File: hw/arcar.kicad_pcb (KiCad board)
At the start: 2 copper layers, 74 parts, among them J1 USB_B_Micro, J2 GPIO, J3 MOTOR, J4 POWER, M1 screw, M2 screw, M3 screw, P1 AVR_ISP_02X03, SW1 SW_Push, U1 USBLC6-2SC6, U10 MCP1826S, U2 ATMEGA328PB-AU, U3 CP2102, U4 ULN2003A, U5 LSM9DS1, U6 ULN2003A, U7 TLE52062GAUMA1, U8 RN4871, U9 MCP16301H

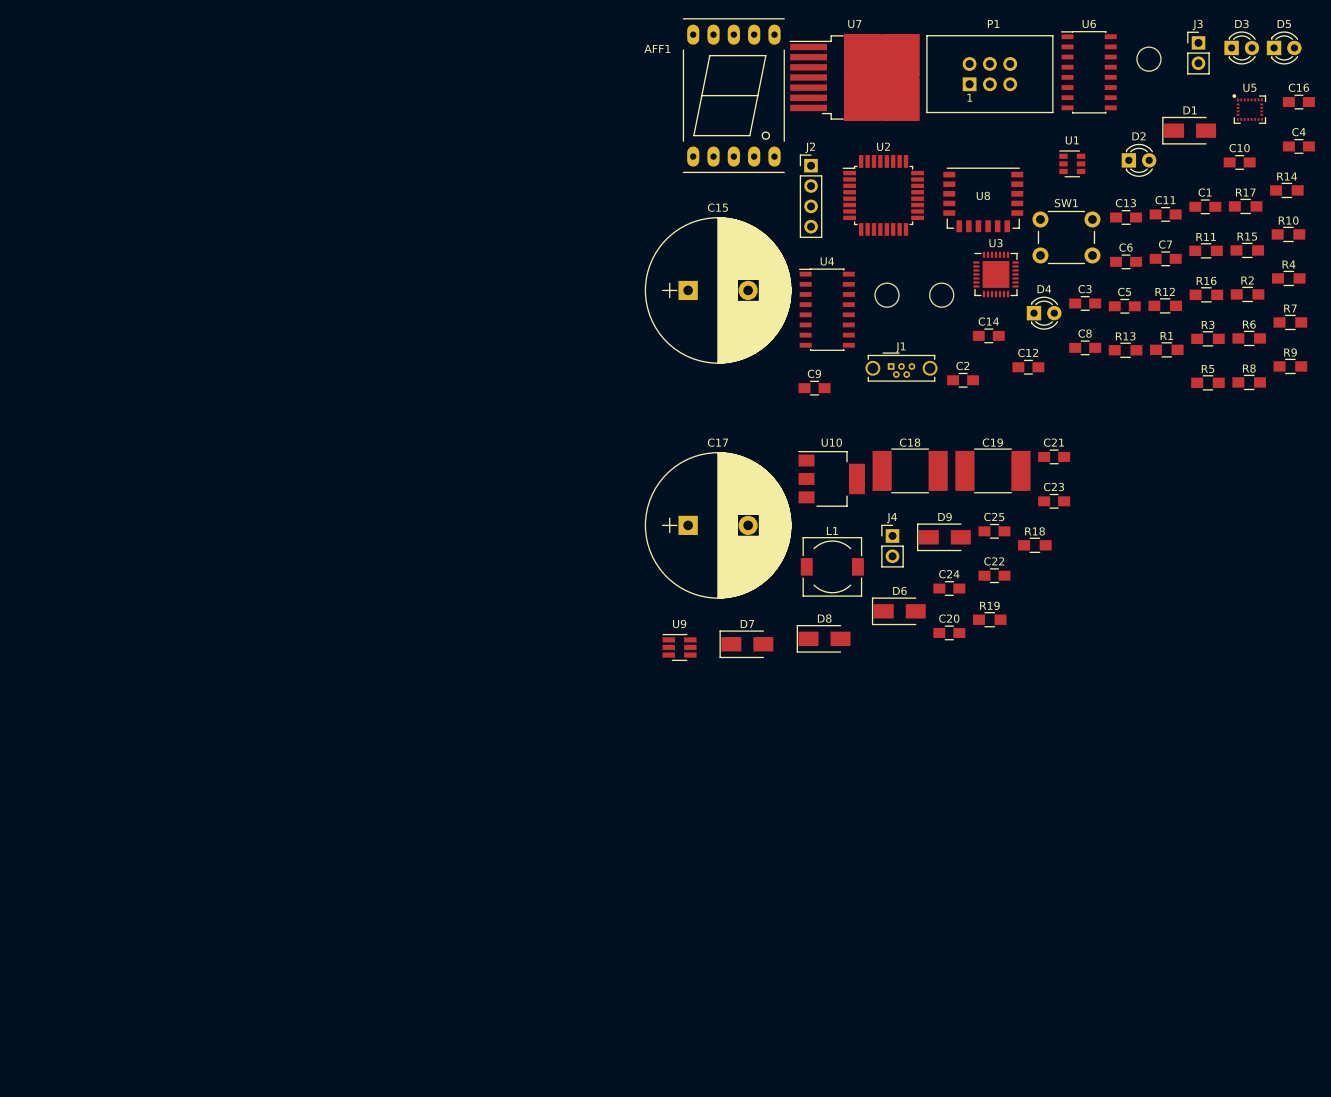
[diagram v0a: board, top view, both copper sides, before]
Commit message: reduced schematic
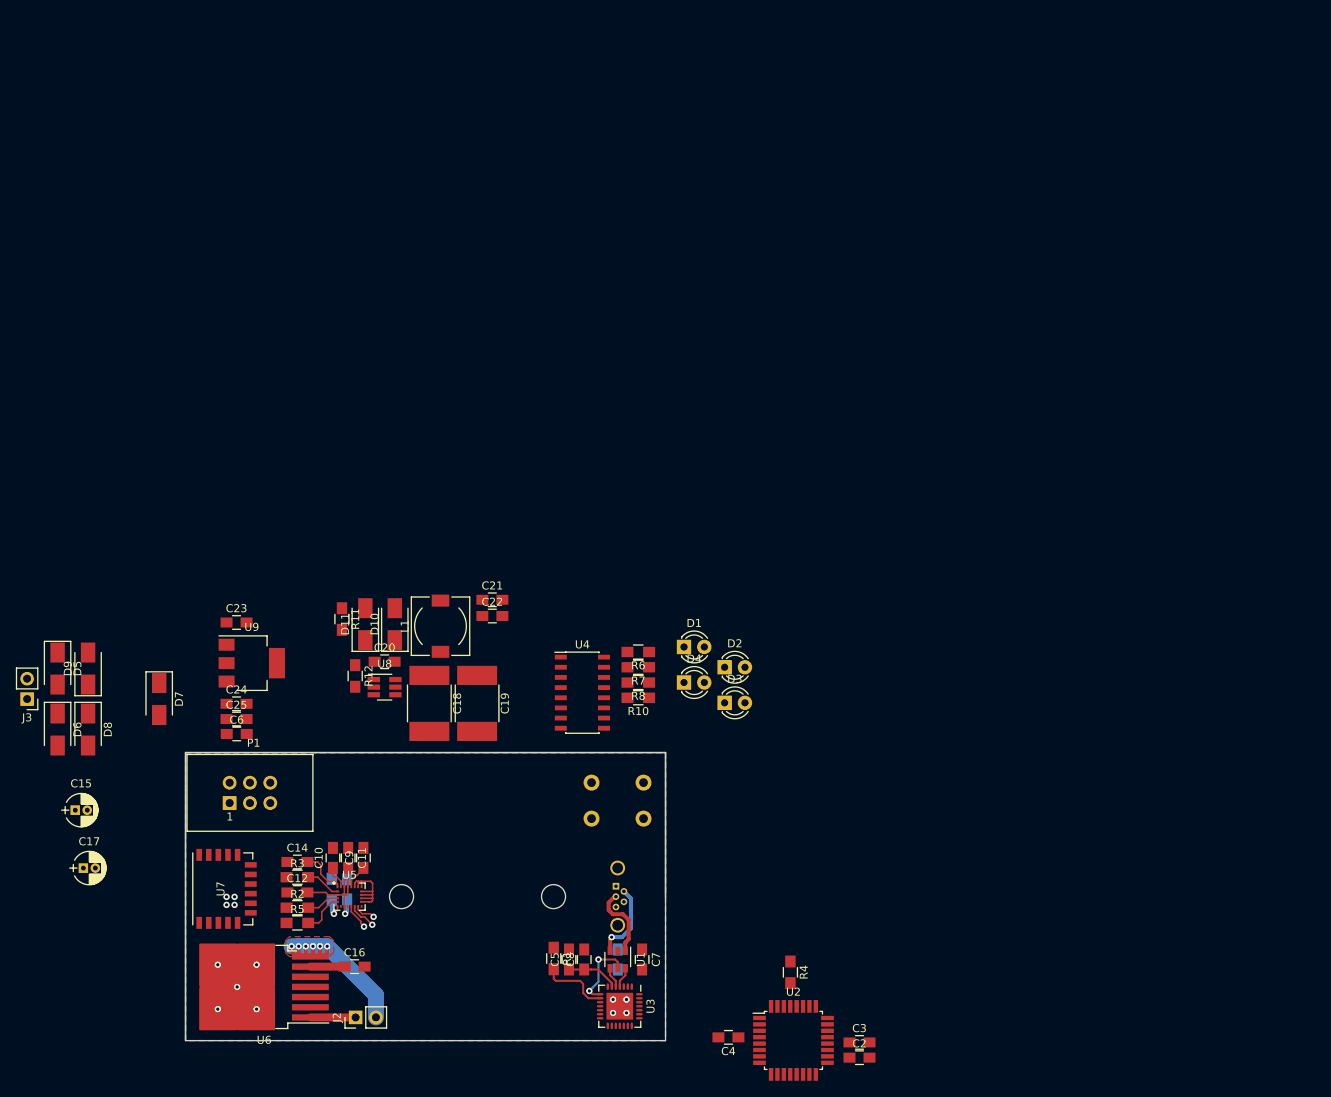
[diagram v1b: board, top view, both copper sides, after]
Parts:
- removed AFF1: LTS-6960HR, Displays_7-Segment:7SegmentLED_LTS6760_LTS6780
- removed J4: POWER, Socket_Strips:Socket_Strip_Straight_1x02_Pitch2.54mm
- removed M3: screw, wyk_mech:screw_M3
- removed R13: 10k, Resistors_SMD:R_0805_HandSoldering
- removed R14, R15, R16, R17: 330R, Resistors_SMD:R_0805_HandSoldering
- removed R18: 330k, Resistors_SMD:R_0805_HandSoldering
- removed R19: 56k, Resistors_SMD:R_0805_HandSoldering
- removed U10: MCP1826S, TO_SOT_Packages_SMD:SOT-223-3Lead_TabPin2
- added D10: SK32SMA, Diodes_SMD:D_SMA, F.Cu at (53.2, 115.9)
- added D11: SK32SMA, Diodes_SMD:D_SMA, F.Cu at (49.5, 115.9)
- C1, C13, J1, SW1: moved to B.Cu
- C15, C17: footprint Capacitors_THT:CP_Radial_D18.0mm_P7.50mm -> Capacitors_THT:CP_Radial_D4.0mm_P1.50mm
- D1: value SK32SMA -> LED; footprint Diodes_SMD:D_SMA -> LEDs:LED_D3.0mm_FlatTop
- D5: value LED -> SK32SMA; footprint LEDs:LED_D3.0mm_FlatTop -> Diodes_SMD:D_SMA
- J2: value GPIO -> MOTOR; footprint Pin_Headers:Pin_Header_Straight_1x04_Pitch2.54mm -> Pin_Headers:Pin_Header_Straight_1x02_Pitch2.54mm
- J3: value MOTOR -> POWER
- R11: value 330R -> 220k
- R12: value 330R -> 22k
- R2: value 10k -> 4k7
- R4: value 4k7 -> 10k
- R9: value 330R -> 10k; moved to B.Cu
- U6: value ULN2003A -> TLE52062GAUMA1; footprint Housings_SOIC:SOIC-16_3.9x9.9mm_Pitch1.27mm -> TO_SOT_Packages_SMD:TO-263-7_TabPin4
- U7: value TLE52062GAUMA1 -> RN4871; footprint TO_SOT_Packages_SMD:TO-263-7_TabPin4 -> wyk_rf_modules:RN4871
- U8: value RN4871 -> MCP16301H; footprint wyk_rf_modules:RN4871 -> TO_SOT_Packages_SMD:SOT-23-6_Handsoldering
- U9: value MCP16301H -> MCP1826S; footprint TO_SOT_Packages_SMD:SOT-23-6_Handsoldering -> TO_SOT_Packages_SMD:SOT-223-3Lead_TabPin2
- moved D5 170.7 mm to (11.0, 121.5), turned to 270 degrees
- moved J3 167.8 mm to (7.20, 125.3), turned to 180 degrees
- moved C16 160.0 mm to (48.1, 158.8)
- moved U6 154.0 mm to (36.8, 161.3), turned to 180 degrees
- moved U5 149.5 mm to (47.5, 150.0)
- moved C10 142.8 mm to (45.4, 145.2), turned to 90 degrees
- moved R2 141.4 mm to (41.0, 151.4)
- moved R9 136.5 mm to (45.3, 149.1), turned to 270 degrees
- moved R5 132.3 mm to (41.0, 153.3)
- moved C4 132.2 mm to (94.9, 167.6), turned to 180 degrees
- moved R3 132.2 mm to (41.0, 147.6)
- moved C11 130.0 mm to (47.3, 145.2), turned to 270 degrees
- moved P1 128.9 mm to (32.5, 138.3)
- moved C13 128.6 mm to (47.2, 149.1), turned to 270 degrees
- moved M2 128.4 mm to (73.0, 150.0)
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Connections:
- net Net-(J1-Pad2) renamed /D-
- net Net-(J1-Pad3) renamed /D+
- net Net-(U1-Pad4) renamed /D2-
- net Net-(U1-Pad6) renamed /D2+
- C21 pad 1: +5V5 -> +5V
- C22 pad 1: +5V5 -> +5V
- C23 pad 1: +5V5 -> +5V
- D1 pad 1: +5V5 -> Net-(D1-Pad1)
- D1 pad 2: Net-(D1-Pad2) -> VCC
- D5 pad 1: Net-(D5-Pad1) -> VCC
- D5 pad 2: VCC -> Net-(D5-Pad2)
- D6 pad 1: VCC -> Net-(D5-Pad2)
- D6 pad 2: Net-(D6-Pad2) -> GND
- D7 pad 1: Net-(C17-Pad1) -> VCC
- D7 pad 2: VCC -> Net-(D7-Pad2)
- D8 pad 1: Net-(C20-Pad2) -> Net-(D7-Pad2)
- D9 pad 1: Net-(C20-Pad1) -> Net-(C17-Pad1)
- D9 pad 2: +5V5 -> VCC
- J2 pad 1: /GPIO1 -> Net-(J2-Pad1)
- J2 pad 2: /GPIO2 -> Net-(J2-Pad2)
- J3 pad 1: Net-(J3-Pad1) -> Net-(D7-Pad2)
- J3 pad 2: Net-(J3-Pad2) -> Net-(D5-Pad2)
- L1 pad 2: +5V5 -> +5V
- P1 pad 2: Net-(D1-Pad2) -> +5V
- R10 pad 1: Net-(AFF1-Pad1) -> Net-(D4-Pad1)
- R11 pad 1: Net-(AFF1-Pad9) -> +5V
- R12 pad 1: Net-(AFF1-Pad10) -> Net-(R11-Pad2)
- R12 pad 2: Net-(R12-Pad2) -> GND
- R2 pad 2: /~RST -> /SDA
- R3 pad 2: /SDA -> /SCL
- R4 pad 2: /SCL -> /~RST
- R6 pad 1: Net-(AFF1-Pad7) -> Net-(D1-Pad1)
- R7 pad 1: Net-(AFF1-Pad6) -> Net-(D2-Pad1)
- R8 pad 1: Net-(AFF1-Pad4) -> Net-(D3-Pad1)
- R9 pad 1: Net-(AFF1-Pad2) -> +3V3
- U2 pad 10: /SEG_D -> Net-(U2-Pad10)
- U2 pad 11: /SEG_E -> Net-(U2-Pad11)
- U2 pad 19: /SEG_F -> Net-(U2-Pad19)
- U2 pad 22: /SEG_G -> Net-(U2-Pad22)
- U2 pad 3: /SEG_A -> Net-(U2-Pad3)
- U2 pad 6: /SEG_B -> Net-(U2-Pad6)
- U2 pad 7: /GPIO1 -> Net-(U2-Pad7)
- U2 pad 8: /GPIO2 -> Net-(U2-Pad8)
- U2 pad 9: /SEG_C -> Net-(U2-Pad9)
- U3 pad 7: +5V -> Net-(U3-Pad7)
- U4 pad 1: /SEG_A -> /FL_LED
- U4 pad 10: Net-(R12-Pad2) -> Net-(U4-Pad10)
- U4 pad 11: Net-(R11-Pad2) -> Net-(U4-Pad11)
- U4 pad 12: Net-(R10-Pad2) -> Net-(U4-Pad12)
- U4 pad 13: Net-(R9-Pad2) -> Net-(R10-Pad2)
- U4 pad 2: /SEG_B -> /FR_LED
- U4 pad 3: /SEG_C -> /BL_LED
- U4 pad 4: /SEG_D -> /BR_LED
- U4 pad 5: /SEG_E -> GND
- U4 pad 6: /SEG_F -> GND
- U4 pad 7: /SEG_G -> GND
- U4 pad 9: VCC -> Net-(U4-Pad9)
- U5 pad 6: Net-(R13-Pad2) -> Net-(R9-Pad2)
- U6 pad 1: /FL_LED -> Net-(J2-Pad1)
- U6 pad 2: /FR_LED -> /MOTOR_ERR
- U6 pad 3: /BL_LED -> /MOTOR_PWM1
- U6 pad 4: /BR_LED -> GND
- U6 pad 5: GND -> /MOTOR_PWM2
- U6 pad 6: GND -> VCC
- U6 pad 7: GND -> Net-(J2-Pad2)
- U7 pad 1: Net-(J3-Pad1) -> Net-(U7-Pad1)
- U7 pad 2: /MOTOR_ERR -> GND
- U7 pad 3: /MOTOR_PWM1 -> Net-(U7-Pad3)
- U7 pad 4: GND -> Net-(U7-Pad4)
- U7 pad 5: /MOTOR_PWM2 -> Net-(U7-Pad5)
- U7 pad 6: VCC -> Net-(U7-Pad6)
- U7 pad 7: Net-(J3-Pad2) -> /TX
- U8 pad 1: Net-(U8-Pad1) -> Net-(C20-Pad1)
- U8 pad 3: Net-(U8-Pad3) -> Net-(R11-Pad2)
- U8 pad 4: Net-(U8-Pad4) -> Net-(C17-Pad1)
- U8 pad 5: Net-(U8-Pad5) -> Net-(C17-Pad1)
- U8 pad 6: Net-(U8-Pad6) -> Net-(C20-Pad2)
- U9 pad 1: Net-(C20-Pad1) -> +5V
- U9 pad 3: Net-(R18-Pad2) -> +3V3
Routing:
- net GND: track 0.00 -> 37.2 mm, vias 0 -> 13
- net Net-(J2-Pad2): track 0.00 -> 30.7 mm, vias 0 -> 6
- net +3V3: track 0.00 -> 27.9 mm, vias 0 -> 1
- net /D-: track 0.00 -> 9.61 mm, vias 0 -> 1
- net +5V: track 0.00 -> 9.25 mm, vias 0 -> 2
- net /D+: track 0.00 -> 9.20 mm
- net Net-(R1-Pad2): track 0.00 -> 8.67 mm
- net Net-(J2-Pad1): track 0.00 -> 5.66 mm
- net Net-(R5-Pad2): track 0.00 -> 5.38 mm
- net /SCL: track 0.00 -> 4.43 mm
- net VCC: track 0.00 -> 4.28 mm
- net /SDA: track 0.00 -> 4.18 mm
- net /INT1_A/G: track 0.00 -> 3.46 mm, vias 0 -> 1
- net /INT_M: track 0.00 -> 3.19 mm, vias 0 -> 1
- net Net-(C10-Pad1): track 0.00 -> 3.08 mm
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- added copper zone on B.Cu, net GND
- added copper zone on F.Cu, net GND
- added copper zone on F.Cu, net Net-(J2-Pad2)
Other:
- board outline added: 60 x 36 mm

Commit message: big reduced change all power source
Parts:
- removed C20, C23, C24: 100n, Capacitors_SMD:C_0805_HandSoldering
- removed C21, C22, C25: 10u, Capacitors_SMD:C_0805_HandSoldering
- removed D10, D11: SK32SMA, Diodes_SMD:D_SMA
- removed L1: DE0704-22, Choke_SMD:Choke_SMD_7.3x7.3_H4.5
- removed R11: 220k, Resistors_SMD:R_0805_HandSoldering
- removed R12: 22k, Resistors_SMD:R_0805_HandSoldering
- removed U9: MCP1826S, TO_SOT_Packages_SMD:SOT-223-3Lead_TabPin2
- C18, C19: value 10u -> 1u/50V; footprint Capacitors_SMD:C_2220_HandSoldering -> Capacitors_SMD:C_0805_HandSoldering
- U8: value MCP16301H -> MCP1804T-3302I/DB; footprint TO_SOT_Packages_SMD:SOT-23-6_Handsoldering -> TO_SOT_Packages_SMD:SOT-223
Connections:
- C1 pad 1: +5V -> VCC
- C19 pad 1: Net-(C17-Pad1) -> +3V3
- J1 pad 1: +5V -> VCC
- P1 pad 2: +5V -> VCC
- R1 pad 1: +5V -> VCC
- U1 pad 5: +5V -> VCC
- U3 pad 8: +5V -> VCC
- U8 pad 1: Net-(C20-Pad1) -> Net-(C17-Pad1)
- U8 pad 3: Net-(R11-Pad2) -> +3V3
- U8 pad 4: Net-(C17-Pad1) -> (no net)
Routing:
- net +5V: track 9.25 -> 0.00 mm, vias 2 -> 0
- net VCC: track 4.28 -> 13.5 mm, vias 0 -> 2

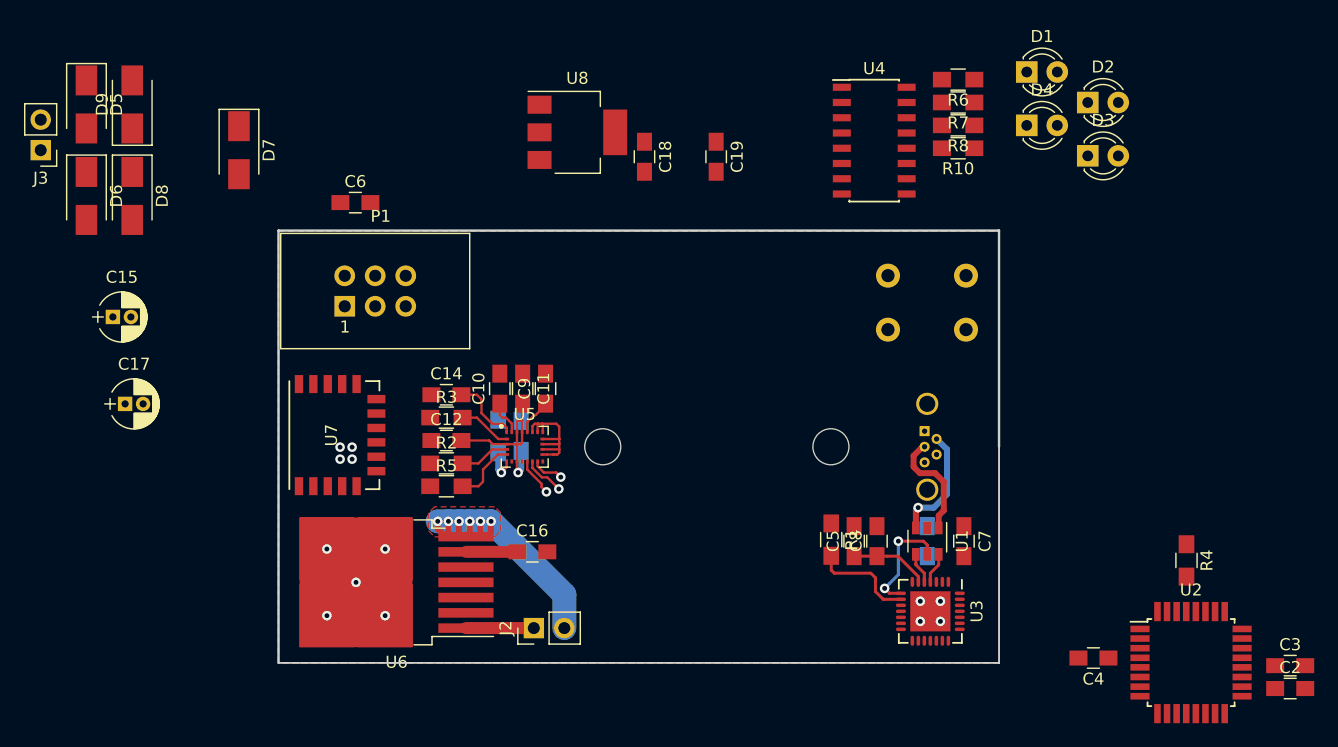
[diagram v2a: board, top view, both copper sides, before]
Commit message: all the components are placed on the board
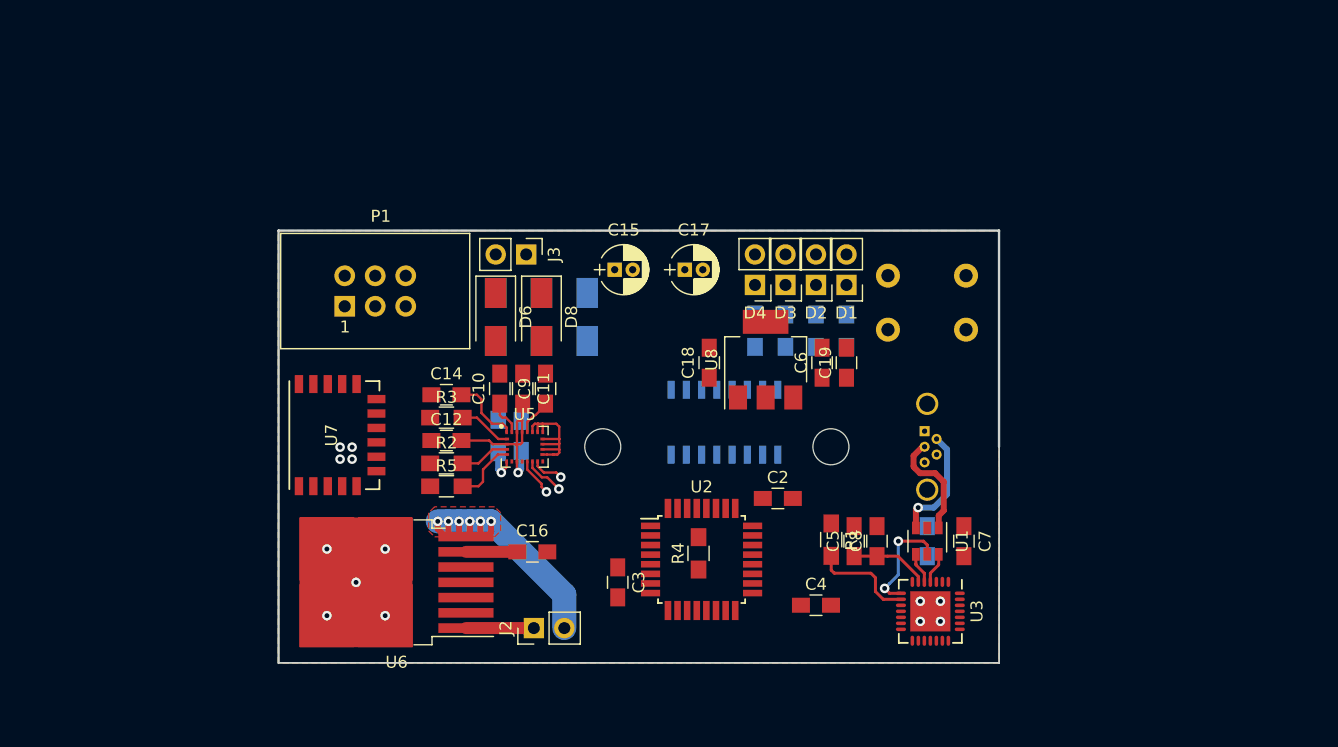
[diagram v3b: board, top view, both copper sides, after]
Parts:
- D1, D2, D3, D4: footprint LEDs:LED_D3.0mm_FlatTop -> Pin_Headers:Pin_Header_Straight_1x02_Pitch2.54mm
- D5, D7, D9, R10, R6, R7, R8, U4: moved to B.Cu
- moved C3 56.4 mm to (55.2, 161.3), turned to 270 degrees
- moved C17 47.9 mm to (60.8, 135.3)
- moved C2 45.5 mm to (68.6, 154.3)
- moved C15 42.0 mm to (55.0, 135.3)
- moved D9 41.8 mm to (52.7, 139.2), turned to 270 degrees
- moved U2 41.7 mm to (62.2, 159.4)
- moved J3 41.3 mm to (47.6, 134.0), turned to 270 degrees
- moved C6 41.1 mm to (72.3, 143.0), turned to 90 degrees
- moved R4 40.6 mm to (62.0, 158.9), turned to 90 degrees
- moved D5 38.4 mm to (45.1, 139.2), turned to 90 degrees
- moved D6 35.5 mm to (45.1, 139.2)
- moved D8 35.5 mm to (48.9, 139.2)
- moved D7 28.8 mm to (48.9, 139.2), turned to 90 degrees
- moved D3 27.4 mm to (69.2, 136.5), turned to 180 degrees
- moved D2 27.3 mm to (71.8, 136.5), turned to 180 degrees
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
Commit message: all routed
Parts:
- C2, C3, C4, D6, D8, R4: moved to B.Cu
- U8: footprint TO_SOT_Packages_SMD:SOT-223 -> TO_SOT_Packages_SMD:SOT-223-3_TabPin2
- moved R4 27.1 mm to (40.0, 142.9)
- moved D6 15.7 mm to (60.5, 142.3), turned to 0 degrees
- moved D8 11.6 mm to (60.5, 138.8), turned to 0 degrees
- moved C4 7.05 mm to (64.9, 161.5), turned to 180 degrees
- moved C2 6.59 mm to (64.9, 159.8), turned to 180 degrees
- moved C3 5.00 mm to (59.7, 159.0), turned to 0 degrees
- moved C15 0.40 mm to (55.1, 135.6)
- moved C17 0.40 mm to (61.0, 135.6)
- moved C13 0.10 mm to (47.2, 149.0), turned to 90 degrees
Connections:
- U2 pad 13: /MOTOR_PWM1 -> /MOTOR_PWM2
- U2 pad 14: /MOTOR_PWM2 -> /MOTOR_PWM1
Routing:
- net VCC: track 13.5 -> 153.1 mm, vias 2 -> 6
- net +3V3: track 27.9 -> 153.2 mm, vias 1 -> 6
- net /~RST: track 0.00 -> 124.4 mm, vias 0 -> 2
- net /MISO: track 0.00 -> 102.8 mm, vias 0 -> 3
- net /MOSI: track 0.00 -> 87.2 mm, vias 0 -> 3
- net /SCK: track 0.00 -> 72.3 mm, vias 0 -> 1
- net /RX: track 0.00 -> 41.3 mm
- net /TX: track 0.00 -> 40.6 mm
- net /SCL: track 4.43 -> 34.7 mm, vias 0 -> 2
- net Net-(C17-Pad1): track 0.00 -> 27.3 mm
- net /SDA: track 4.18 -> 30.2 mm, vias 0 -> 2
- net /MOTOR_PWM1: track 0.00 -> 24.5 mm
- net /MOTOR_PWM2: track 0.00 -> 24.3 mm
- net /MOTOR_ERR: track 0.00 -> 23.4 mm, vias 0 -> 2
- net Net-(D5-Pad2): track 0.00 -> 22.7 mm, vias 0 -> 3
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
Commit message: PCB upgraded
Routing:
- net /MISO: track 102.8 -> 106.5 mm
- net VCC: track 153.1 -> 156.2 mm
- net GND: track 41.1 -> 44.2 mm
- net /~RST: track 124.4 -> 126.1 mm
- net +3V3: track 153.2 -> 151.8 mm
- net /SCK: track 72.3 -> 71.1 mm, vias 1 -> 2
- net /RX: track 41.3 -> 40.3 mm
- net /SCL: track 34.7 -> 33.7 mm
- net /MOTOR_PWM2: track 24.3 -> 25.0 mm
- net /MOSI: track 87.2 -> 87.8 mm
- net /TX: track 40.6 -> 40.0 mm
